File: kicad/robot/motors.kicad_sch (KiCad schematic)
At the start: 15 parts, among them J3 67996-412HLF, Q6 SN74AHC125RGYR, U8 DRV8830DRCR, U9 DRV8830DRCR

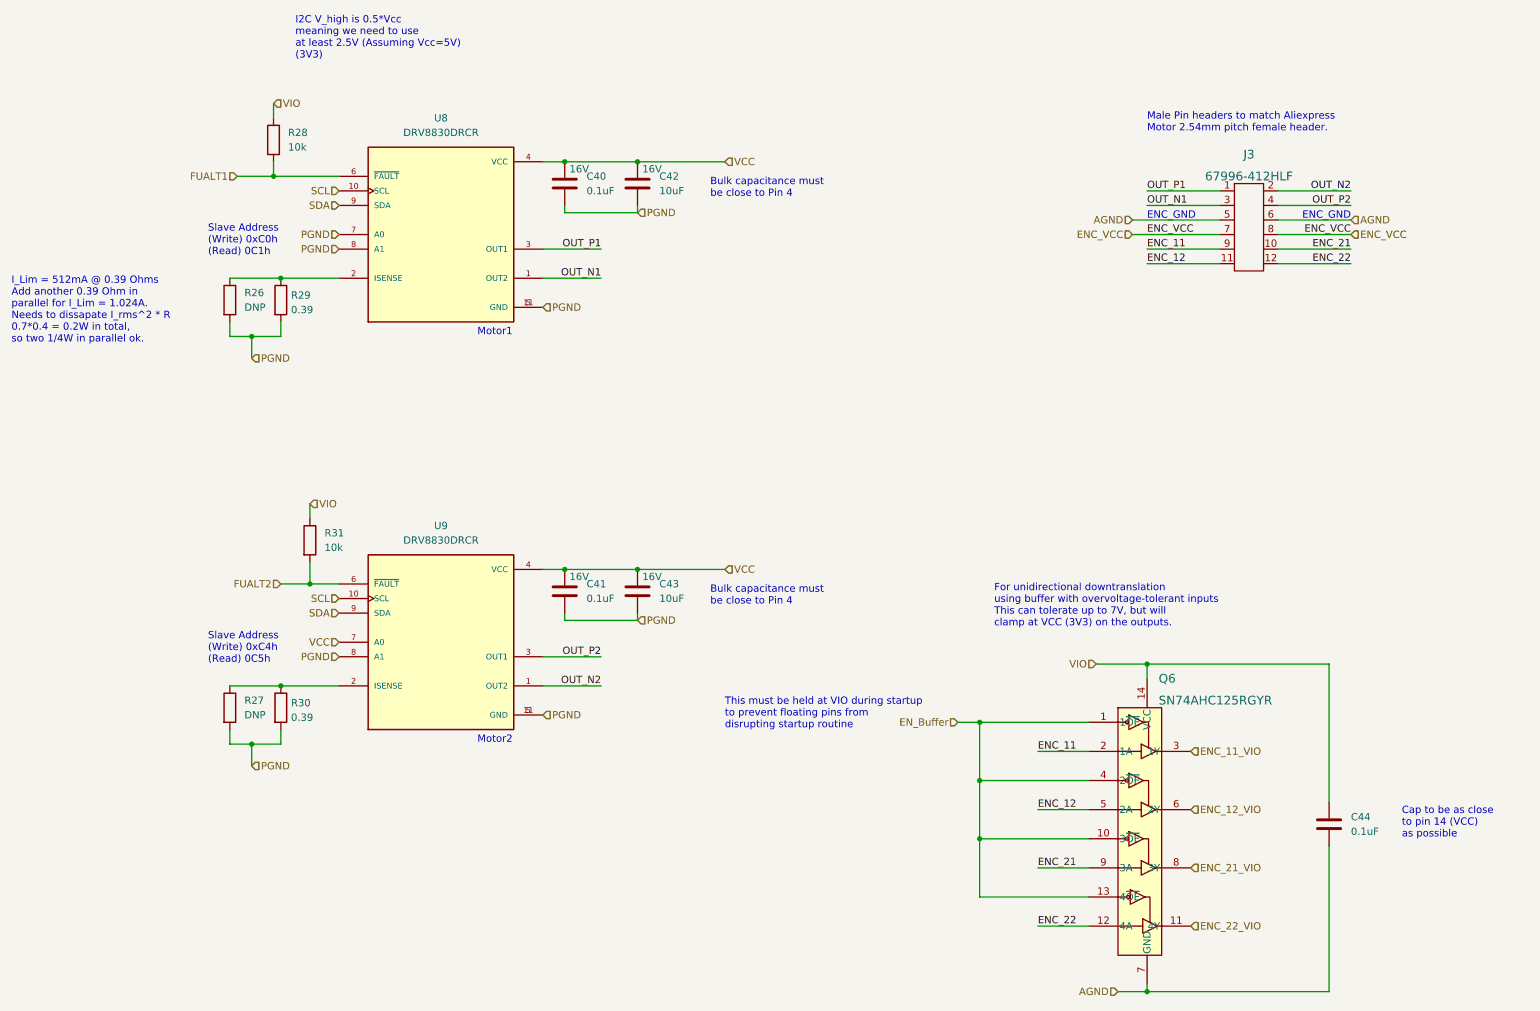
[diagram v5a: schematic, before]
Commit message: Bulk capacitor field edits
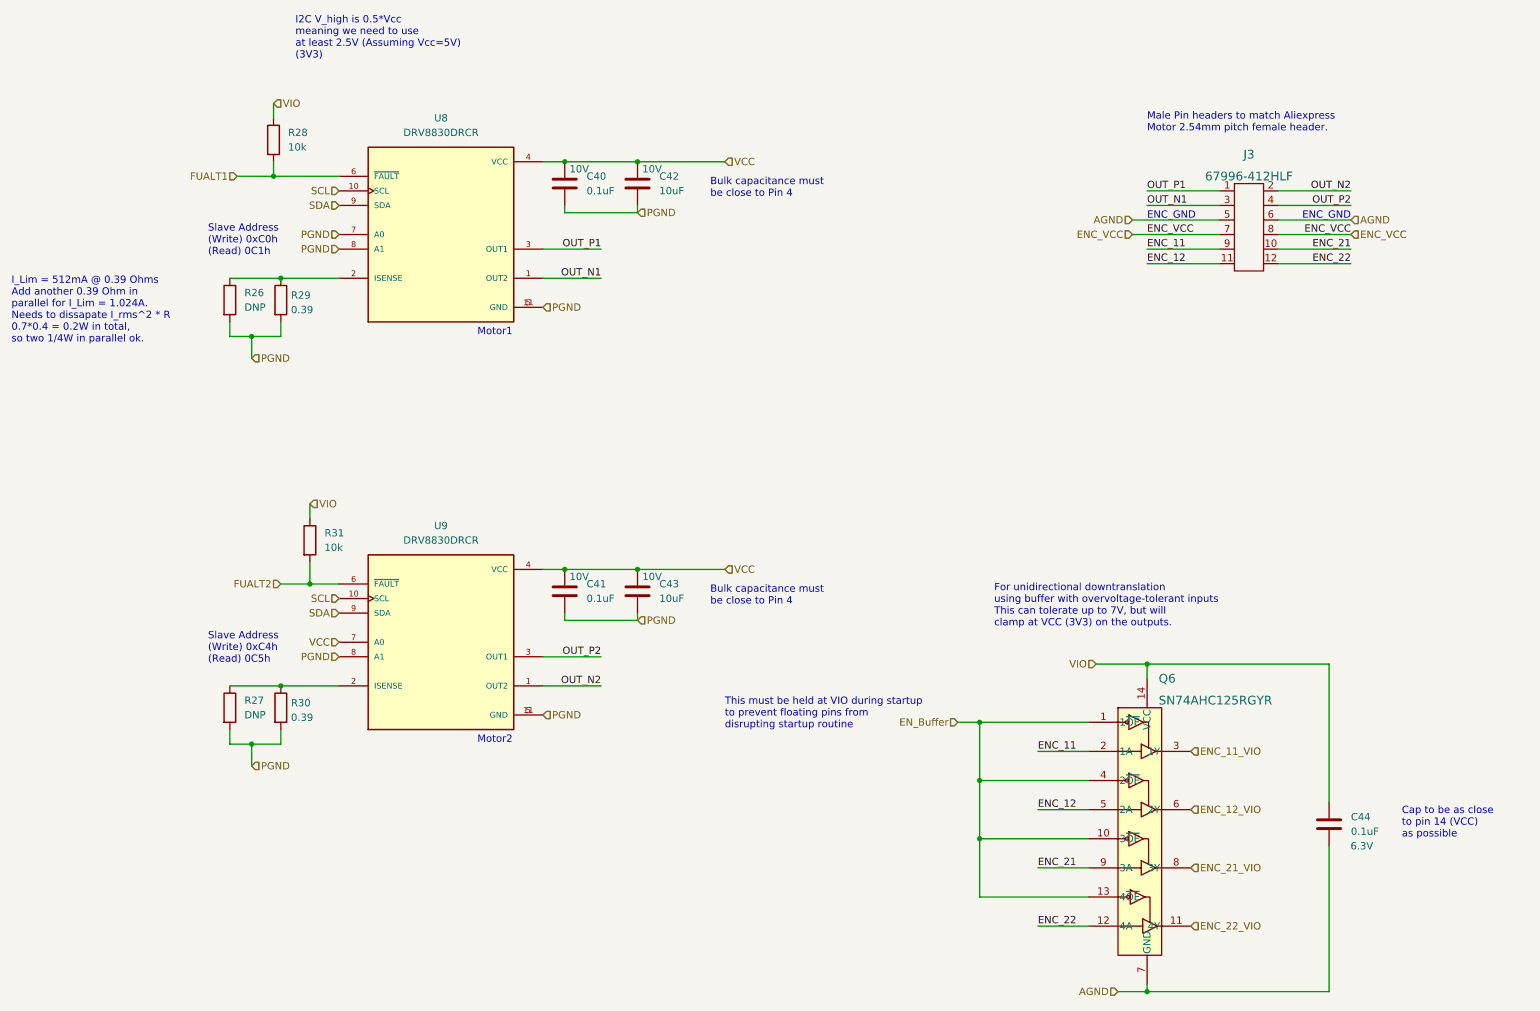
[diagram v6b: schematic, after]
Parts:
- C40, C41: Manufacturer Samsung -> (none); Part Number CL21B104MACNNNC -> (none)
- C42, C43: Manufacturer Samsung -> (none); Part Number CL21A106KOQNNNG -> (none)
- C44: Manufacturer Samsung -> (none); Part Number CL10B104KB8NNWC -> (none)
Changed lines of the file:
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@@
       (effects (font (size 1.27 1.27)) hide)
     )
-    (property "Description" "16V" (id 4) (at 133.35 46.99 0))
-    (property "Manufacturer" "Samsung" (id 5) (at 130.81 49.53 0)
-      (effects (font (size 1.27 1.27)) hide)
-    )
-    (property "Part Number" "CL21A106KOQNNNG" (id 6) (at 130.81 49.53 0)
-      (effects (font (size 1.27 1.27)) hide)
-    )
+    (property "Description" "10V" (id 4) (at 133.35 46.99 0))
     (pin "1")
     (pin "2")
@@
       (effects (font (size 1.27 1.27)) hide)
     )
-    (property "Description" "16V" (id 4) (at 120.65 46.99 0))
-    (property "Manufacturer" "Samsung" (id 5) (at 118.11 49.53 0)
-      (effects (font (size 1.27 1.27)) hide)
-    )
-    (property "Part Number" "CL21B104MACNNNC" (id 6) (at 118.11 49.53 0)
-      (effects (font (size 1.27 1.27)) hide)
-    )
+    (property "Description" "10V" (id 4) (at 120.65 46.99 0))
     (pin "1")
     (pin "2")
@@
       (effects (font (size 1.27 1.27)) hide)
     )
-    (property "Description" "16V" (id 4) (at 133.35 118.11 0))
-    (property "Manufacturer" "Samsung" (id 5) (at 130.81 120.65 0)
-      (effects (font (size 1.27 1.27)) hide)
-    )
-    (property "Part Number" "CL21A106KOQNNNG" (id 6) (at 130.81 120.65 0)
-      (effects (font (size 1.27 1.27)) hide)
-    )
+    (property "Description" "10V" (id 4) (at 133.35 118.11 0))
     (pin "1")
     (pin "2")
@@
       (effects (font (size 1.27 1.27)) hide)
     )
-    (property "Description" "16V" (id 4) (at 120.65 118.11 0))
-    (property "Manufacturer" "Samsung" (id 5) (at 118.11 120.65 0)
-      (effects (font (size 1.27 1.27)) hide)
-    )
-    (property "Part Number" "CL21B104MACNNNC" (id 6) (at 118.11 120.65 0)
-      (effects (font (size 1.27 1.27)) hide)
-    )
+    (property "Description" "10V" (id 4) (at 120.65 118.11 0))
     (pin "1")
     (pin "2")
@@
   )
   (symbol (lib_id "Device:C") (at 251.46 161.29 0) (unit 1)
-    (in_bom yes) (on_board yes) (fields_autoplaced)
+    (in_bom yes) (on_board yes)
     (property "Reference" "C44" (id 0) (at 255.27 160.0199 0)
       (effects (font (size 1.27 1.27)) (justify left))
@@
       (effects (font (size 1.27 1.27)) hide)
     )
-    (property "Manufacturer" "Samsung" (id 4) (at 251.46 161.29 0)
-      (effects (font (size 1.27 1.27)) hide)
-    )
-    (property "Part Number" "CL10B104KB8NNWC" (id 5) (at 251.46 161.29 0)
-      (effects (font (size 1.27 1.27)) hide)
-    )
-    (pin "1")
-    (pin "2")
+    (property "Description" "6.3V" (id 4) (at 257.175 165.1 0))
+    (pin "1")
+    (pin "2")

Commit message: bulk footprint updates to capacitors
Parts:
- C40, C41: footprint Capacitor_SMD:C_0805_2012Metric -> Capacitor_SMD:C_0402_1005Metric
- C42, C43: footprint Capacitor_SMD:C_0805_2012Metric -> Capacitor_SMD:C_0603_1608Metric
- C44: footprint Capacitor_SMD:C_0603_1608Metric -> Capacitor_SMD:C_0402_1005Metric
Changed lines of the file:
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@@
       (effects (font (size 1.27 1.27)) (justify left))
     )
-    (property "Footprint" "Capacitor_SMD:C_0805_2012Metric" (id 2) (at 131.7752 53.34 0)
+    (property "Footprint" "Capacitor_SMD:C_0603_1608Metric" (id 2) (at 131.7752 53.34 0)
       (effects (font (size 1.27 1.27)) hide)
     )
@@
       (effects (font (size 1.27 1.27)) (justify left))
     )
-    (property "Footprint" "Capacitor_SMD:C_0805_2012Metric" (id 2) (at 119.0752 53.34 0)
+    (property "Footprint" "Capacitor_SMD:C_0402_1005Metric" (id 2) (at 119.0752 53.34 0)
       (effects (font (size 1.27 1.27)) hide)
     )
@@
       (effects (font (size 1.27 1.27)) (justify left))
     )
-    (property "Footprint" "Capacitor_SMD:C_0805_2012Metric" (id 2) (at 131.7752 124.46 0)
+    (property "Footprint" "Capacitor_SMD:C_0603_1608Metric" (id 2) (at 131.7752 124.46 0)
       (effects (font (size 1.27 1.27)) hide)
     )
@@
       (effects (font (size 1.27 1.27)) (justify left))
     )
-    (property "Footprint" "Capacitor_SMD:C_0805_2012Metric" (id 2) (at 119.0752 124.46 0)
+    (property "Footprint" "Capacitor_SMD:C_0402_1005Metric" (id 2) (at 119.0752 124.46 0)
       (effects (font (size 1.27 1.27)) hide)
     )
@@
       (effects (font (size 1.27 1.27)) (justify left))
     )
-    (property "Footprint" "Capacitor_SMD:C_0603_1608Metric" (id 2) (at 252.4252 165.1 0)
-      (effects (font (size 1.27 1.27)) hide)
-    )
+    (property "Footprint" "Capacitor_SMD:C_0402_1005Metric" (id 2) (at 252.4252 165.1 0)
+      (effects (font (size 1.27 1.27)) hide)
+    )

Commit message: Bulk BOM edits and one replaced footprint for U15
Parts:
- C40, C41, C44: Manufacturer (none) -> Samsung; Part Number (none) -> CL05A104KA5NNNC
- C42, C43: Manufacturer (none) -> Murata; Part Number (none) -> GRM188R61E106KA73J
- R26, R27: Manufacturer Panasonic -> N/A; Part Number ERJ-3RQJR39V -> N/A
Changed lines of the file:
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@@
       (effects (font (size 1.27 1.27)) hide)
     )
-    (property "Manufacturer" "Panasonic" (id 5) (at 59.69 140.97 0)
-      (effects (font (size 1.27 1.27)) hide)
-    )
-    (property "Part Number" "ERJ-3RQJR39V" (id 6) (at 59.69 140.97 0)
+    (property "Manufacturer" "N/A" (id 5) (at 59.69 140.97 0)
+      (effects (font (size 1.27 1.27)) hide)
+    )
+    (property "Part Number" "N/A" (id 6) (at 59.69 140.97 0)
       (effects (font (size 1.27 1.27)) hide)
     )
@@
     )
     (property "Description" "10V" (id 4) (at 133.35 46.99 0))
+    (property "Manufacturer" "Murata" (id 5) (at 130.81 49.53 0)
+      (effects (font (size 1.27 1.27)) hide)
+    )
+    (property "Part Number" "GRM188R61E106KA73J" (id 6) (at 130.81 49.53 0)
+      (effects (font (size 1.27 1.27)) hide)
+    )
     (pin "1")
     (pin "2")
@@
     )
     (property "Description" "10V" (id 4) (at 120.65 46.99 0))
+    (property "Manufacturer" "Samsung" (id 5) (at 118.11 49.53 0)
+      (effects (font (size 1.27 1.27)) hide)
+    )
+    (property "Part Number" "CL05A104KA5NNNC" (id 6) (at 118.11 49.53 0)
+      (effects (font (size 1.27 1.27)) hide)
+    )
     (pin "1")
     (pin "2")
@@
       (effects (font (size 1.27 1.27)) hide)
     )
-    (property "Manufacturer" "Panasonic" (id 5) (at 59.69 69.85 0)
-      (effects (font (size 1.27 1.27)) hide)
-    )
-    (property "Part Number" "ERJ-3RQJR39V" (id 6) (at 59.69 69.85 0)
+    (property "Manufacturer" "N/A" (id 5) (at 59.69 69.85 0)
+      (effects (font (size 1.27 1.27)) hide)
+    )
+    (property "Part Number" "N/A" (id 6) (at 59.69 69.85 0)
       (effects (font (size 1.27 1.27)) hide)
     )
@@
     )
     (property "Description" "10V" (id 4) (at 133.35 118.11 0))
+    (property "Manufacturer" "Murata" (id 5) (at 130.81 120.65 0)
+      (effects (font (size 1.27 1.27)) hide)
+    )
+    (property "Part Number" "GRM188R61E106KA73J" (id 6) (at 130.81 120.65 0)
+      (effects (font (size 1.27 1.27)) hide)
+    )
     (pin "1")
     (pin "2")
@@
     )
     (property "Description" "10V" (id 4) (at 120.65 118.11 0))
+    (property "Manufacturer" "Samsung" (id 5) (at 118.11 120.65 0)
+      (effects (font (size 1.27 1.27)) hide)
+    )
+    (property "Part Number" "CL05A104KA5NNNC" (id 6) (at 118.11 120.65 0)
+      (effects (font (size 1.27 1.27)) hide)
+    )
     (pin "1")
     (pin "2")
@@
     )
     (property "Description" "6.3V" (id 4) (at 257.175 165.1 0))
-    (pin "1")
-    (pin "2")
+    (property "Manufacturer" "Samsung" (id 5) (at 251.46 161.29 0)
+      (effects (font (size 1.27 1.27)) hide)
+    )
+    (property "Part Number" "CL05A104KA5NNNC" (id 6) (at 251.46 161.29 0)
+      (effects (font (size 1.27 1.27)) hide)
+    )
+    (pin "1")
+    (pin "2")
